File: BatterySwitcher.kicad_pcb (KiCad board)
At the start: 2 copper layers, 2 parts

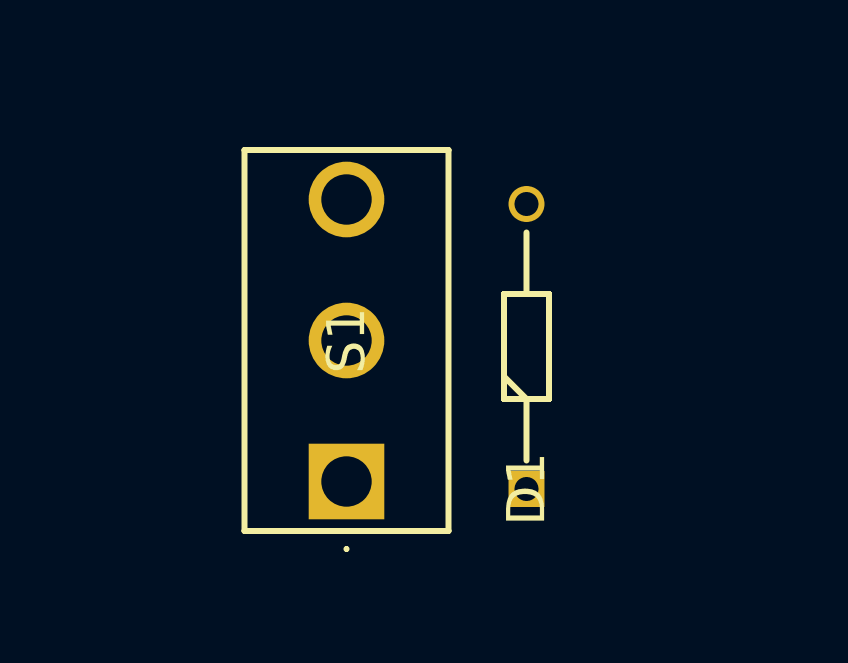
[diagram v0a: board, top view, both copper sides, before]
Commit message: added dip pins for battery and power connections and routing done
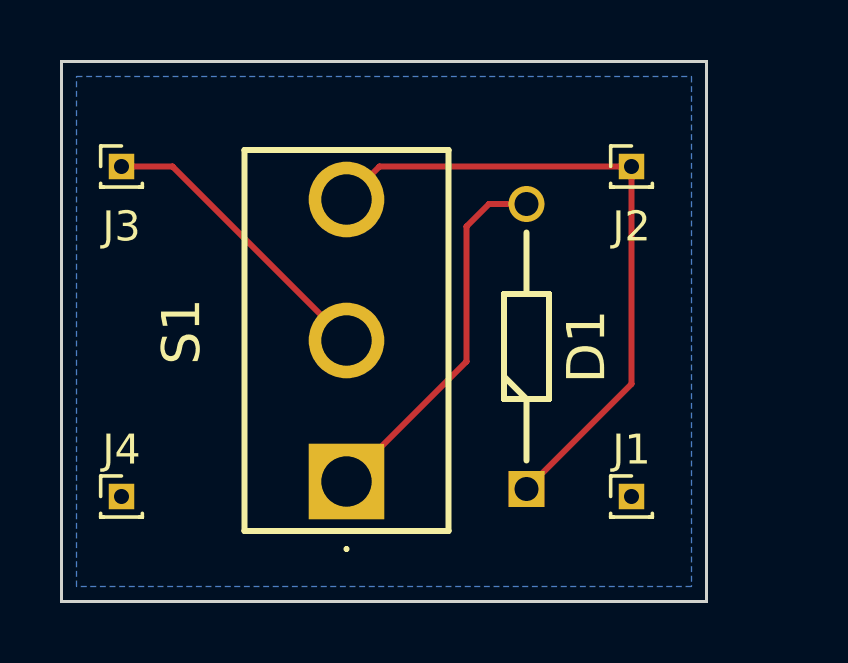
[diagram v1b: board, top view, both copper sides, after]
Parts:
- added J1: Battery -, Connector_PinHeader_1.00mm:PinHeader_1x01_P1.00mm_Vertical, F.Cu at (156.5, 74.0)
- added J2: Battery +, Connector_PinHeader_1.00mm:PinHeader_1x01_P1.00mm_Vertical, F.Cu at (156.5, 63.0)
- added J3: Power +, Connector_PinHeader_1.00mm:PinHeader_1x01_P1.00mm_Vertical, F.Cu at (139.5, 63.0)
- added J4: Power -, Connector_PinHeader_1.00mm:PinHeader_1x01_P1.00mm_Vertical, F.Cu at (139.5, 74.0)
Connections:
- D1 pad 2: unconnected-(D1-Pad2) -> Net-(S1-NC)
- S1 pad 1: unconnected-(S1-NC-Pad1) -> Net-(S1-NC)
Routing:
- net Battery  +: track 0.00 -> 22.2 mm
- net Net-(S1-NC): track 0.00 -> 12.5 mm
- net Power  + : track 0.00 -> 9.90 mm
- added copper zone on B.Cu, net Battery  -
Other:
- board outline added: 21.5 x 18 mm

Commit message: fixed some issues noticed from Miguel Angel
Removed ground plane
Checked copper width for 500mA
Changed diode to shottky with less forward voltage
Added battery connector
Rearrange header pins to be from behind
Reroute all
Added pcb measures
Added part number
Added my signature
Added bill of materials
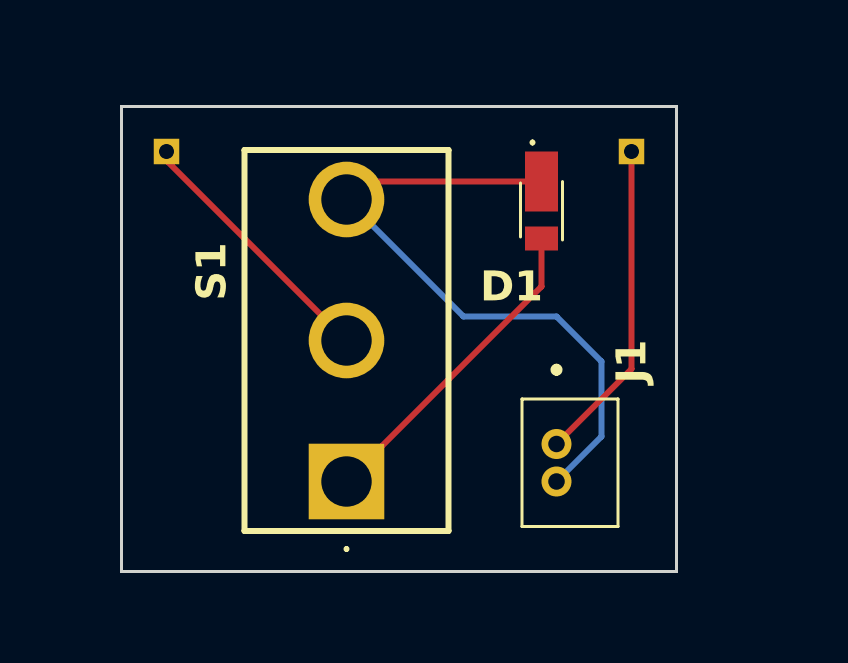
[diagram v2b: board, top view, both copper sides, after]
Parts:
- removed J4: Power -, Connector_PinHeader_1.00mm:PinHeader_1x01_P1.00mm_Vertical
- D1: value 1N4154TAP -> CUHS20S30,H3F; footprint SamacSys_Parts:DIOAD950W60L350D150 -> SamacSys_Parts:CUHS20S40H3F
- J1: value Battery - -> Battery; footprint Connector_PinHeader_1.00mm:PinHeader_1x01_P1.00mm_Vertical -> SamacSys_Parts:530470210
- J2: value Battery + -> Power +; moved to B.Cu
- J3: value Power + -> Power -; moved to B.Cu
- moved J3 17.0 mm to (156.5, 62.5), turned to 180 degrees
- moved J2 15.5 mm to (141.0, 62.5), turned to 180 degrees
- moved D1 9.31 mm to (153.5, 64.5), turned to -90 degrees
- moved J1 3.05 mm to (154.0, 72.2), turned to 90 degrees
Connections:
- J2 pad 1: Battery  + -> Power  + 
- J3 pad 1: Power  +  -> Battery  -
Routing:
- net Battery  -: track 0.00 -> 10.8 mm
- net Net-(D1-A): track 12.5 -> 10.8 mm
- net Power  + : track 9.90 -> 8.79 mm
- removed copper zone on B.Cu, net Battery  -
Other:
- board size 21.5 x 18 mm -> 18.5 x 15.5 mm
- board text added: "BSV01"
- board text added: "Supermanuu"

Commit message: real spacing requirements
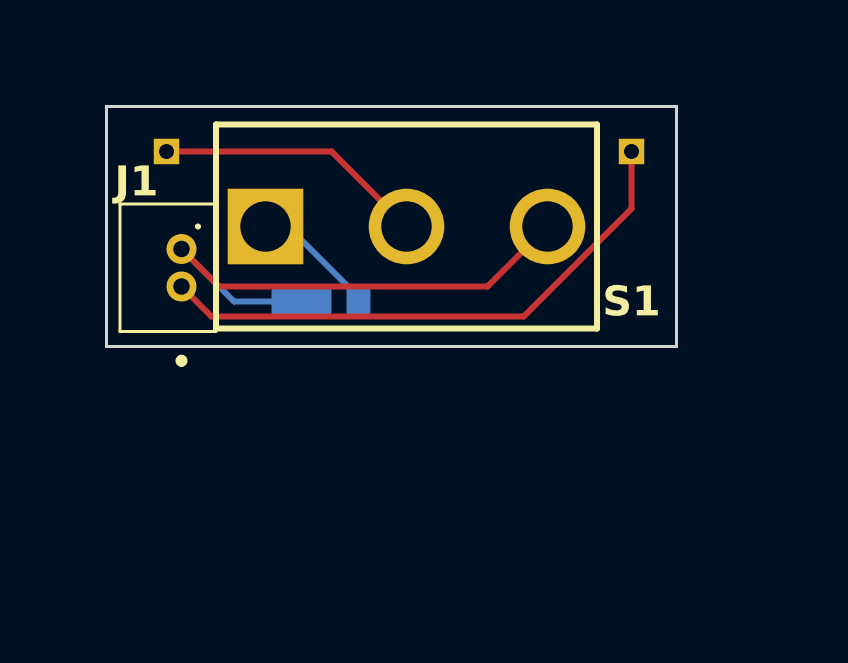
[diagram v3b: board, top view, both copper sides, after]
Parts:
- D1: moved to B.Cu
- moved J1 13.6 mm to (141.5, 67.0), turned to -90 degrees
- moved S1 8.92 mm to (144.3, 65.0), turned to 0 degrees
- moved D1 7.68 mm to (146.4, 67.5), turned to 0 degrees
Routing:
- net Battery  -: track 10.8 -> 18.8 mm
- net Net-(D1-A): track 10.8 -> 4.22 mm
- net Battery  +: track 22.1 -> 18.3 mm
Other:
- board size 18.5 x 15.5 mm -> 19 x 8 mm
- board text removed: "Supermanuu"

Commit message: changed switch by a shorter one
achieved minimum footprint
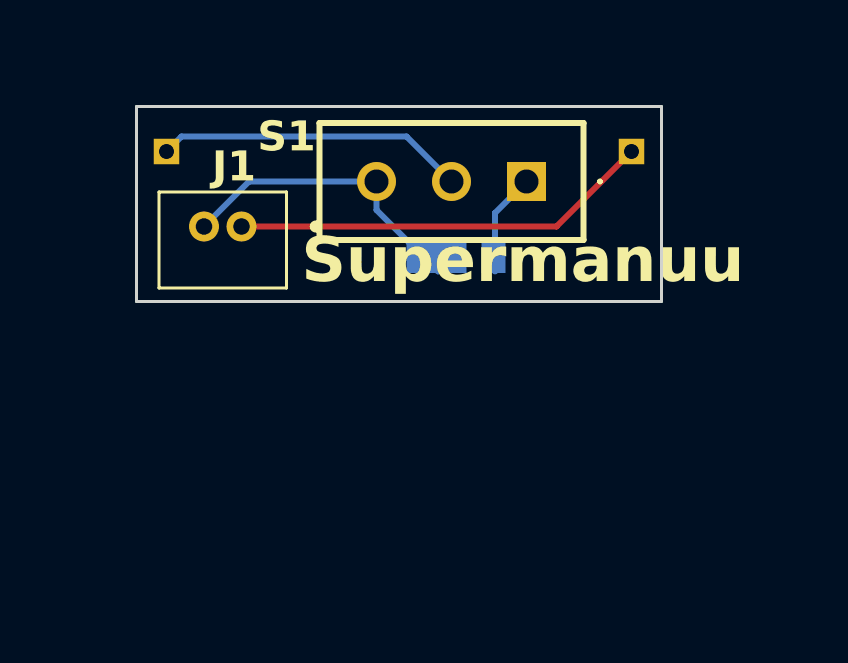
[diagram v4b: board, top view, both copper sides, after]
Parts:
- S1: value SLW-1276864-4A-D -> SLW-883935-2A-D; footprint SamacSys_Parts:SLW12768644AD -> SamacSys_Parts:SLW8839352AD
- moved S1 8.83 mm to (153.0, 63.5), turned to 180 degrees
- moved D1 4.74 mm to (150.9, 66.0)
- moved J1 2.83 mm to (143.5, 65.0), turned to 0 degrees
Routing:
- net Battery  +: track 18.3 -> 10.2 mm
- net Battery  -: track 18.8 -> 14.0 mm
- net Power  + : track 9.04 -> 10.3 mm
- net Net-(D1-A): track 4.22 -> 3.43 mm
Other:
- board size 19 x 8 mm -> 17.5 x 6.5 mm
- board text added: "Supermanuu"
